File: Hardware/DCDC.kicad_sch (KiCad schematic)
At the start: 51 parts, among them Q1 100V 50A, Q2 100V 50A, Q3 100V 50A, Q4 100V 50A, U2 BQ25758A

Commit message: final tweaks before routing traces
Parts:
- C14: value 1u 25V -> 4u7u 25V
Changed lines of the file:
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@@
 	)
 	(junction
-		(at 110.49 107.95)
+		(at 109.22 107.95)
 		(diameter 0)
 		(color 0 0 0 0)
@@
 	(wire
 		(pts
-			(xy 53.34 107.95) (xy 110.49 107.95)
+			(xy 53.34 107.95) (xy 109.22 107.95)
 		)
 		(stroke
@@
 	(wire
 		(pts
-			(xy 110.49 106.68) (xy 110.49 107.95)
+			(xy 109.22 106.68) (xy 109.22 107.95)
 		)
 		(stroke
@@
 	(wire
 		(pts
-			(xy 110.49 107.95) (xy 110.49 109.22)
+			(xy 109.22 107.95) (xy 109.22 109.22)
 		)
 		(stroke
@@
 	(wire
 		(pts
+			(xy 109.22 109.22) (xy 110.49 109.22)
+		)
+		(stroke
+			(width 0)
+			(type default)
+		)
+	)
+	(wire
+		(pts
 			(xy 95.25 27.94) (xy 95.25 29.21)
 		)
@@
 	(wire
 		(pts
+			(xy 109.22 106.68) (xy 110.49 106.68)
+		)
+		(stroke
+			(width 0)
+			(type default)
+		)
+	)
+	(wire
+		(pts
 			(xy 153.67 76.2) (xy 163.83 76.2)
 		)
@@
 	(label "HIDRV1"
 		(at 125.73 91.44 90)
-		(fields_autoplaced yes)
 		(effects
 			(font
@@
 	(label "LODRV2"
 		(at 153.67 91.44 90)
-		(fields_autoplaced yes)
 		(effects
 			(font
@@
 	(label "ACP"
 		(at 105.41 101.6 0)
-		(fields_autoplaced yes)
 		(effects
 			(font
@@
 	(label "VSYS"
 		(at 125.73 29.21 0)
-		(fields_autoplaced yes)
 		(effects
 			(font
@@
 	(label "IIN"
 		(at 179.07 124.46 0)
-		(fields_autoplaced yes)
 		(effects
 			(font
@@
 	(label "SW1"
 		(at 130.81 91.44 90)
-		(fields_autoplaced yes)
 		(effects
 			(font
@@
 	(label "POUT"
 		(at 156.21 29.21 0)
-		(fields_autoplaced yes)
 		(effects
 			(font
@@
 	(label "MODE"
 		(at 179.07 129.54 0)
-		(fields_autoplaced yes)
 		(effects
 			(font
@@
 	(label "HIDRV2"
 		(at 161.29 91.44 90)
-		(fields_autoplaced yes)
 		(effects
 			(font
@@
 	(label "SW2"
 		(at 156.21 91.44 90)
-		(fields_autoplaced yes)
 		(effects
 			(font
@@
 	(label "SRP"
 		(at 179.07 99.06 0)
-		(fields_autoplaced yes)
 		(effects
 			(font
@@
 	(label "ACN"
 		(at 105.41 99.06 0)
-		(fields_autoplaced yes)
 		(effects
 			(font
@@
 	(label "BTST1"
 		(at 128.27 91.44 90)
-		(fields_autoplaced yes)
 		(effects
 			(font
@@
 	(label "LODRV1"
 		(at 133.35 91.44 90)
-		(fields_autoplaced yes)
 		(effects
 			(font
@@
 	(label "IOUT"
 		(at 179.07 127 0)
-		(fields_autoplaced yes)
 		(effects
 			(font
@@
 	(label "BTST2"
 		(at 158.75 91.44 90)
-		(fields_autoplaced yes)
 		(effects
 			(font
@@
 	(label "SRN"
 		(at 179.07 101.6 0)
-		(fields_autoplaced yes)
 		(effects
 			(font
@@
 		(shape input)
 		(at 107.95 137.16 180)
-		(fields_autoplaced yes)
 		(effects
 			(font
@@
 		(shape input)
 		(at 107.95 144.78 180)
-		(fields_autoplaced yes)
 		(effects
 			(font
@@
 		(shape input)
 		(at 257.81 27.94 90)
-		(fields_autoplaced yes)
 		(effects
 			(font
@@
 		(shape input)
 		(at 107.95 139.7 180)
-		(fields_autoplaced yes)
 		(effects
 			(font
@@
 		(shape input)
 		(at 38.1 27.94 90)
-		(fields_autoplaced yes)
 		(effects
 			(font
@@
 		(shape input)
 		(at 187.96 133.35 270)
-		(fields_autoplaced yes)
 		(effects
 			(font
@@
 		(shape input)
 		(at 107.95 142.24 180)
-		(fields_autoplaced yes)
 		(effects
 			(font
@@
 			)
 		)
-		(property "Value" "1u 25V"
+		(property "Value" "4u7u 25V"
 			(at 88.646 127.254 90)
 			(effects
@@
 				)
 				(justify left)
+				(hide yes)
 			)
 		)

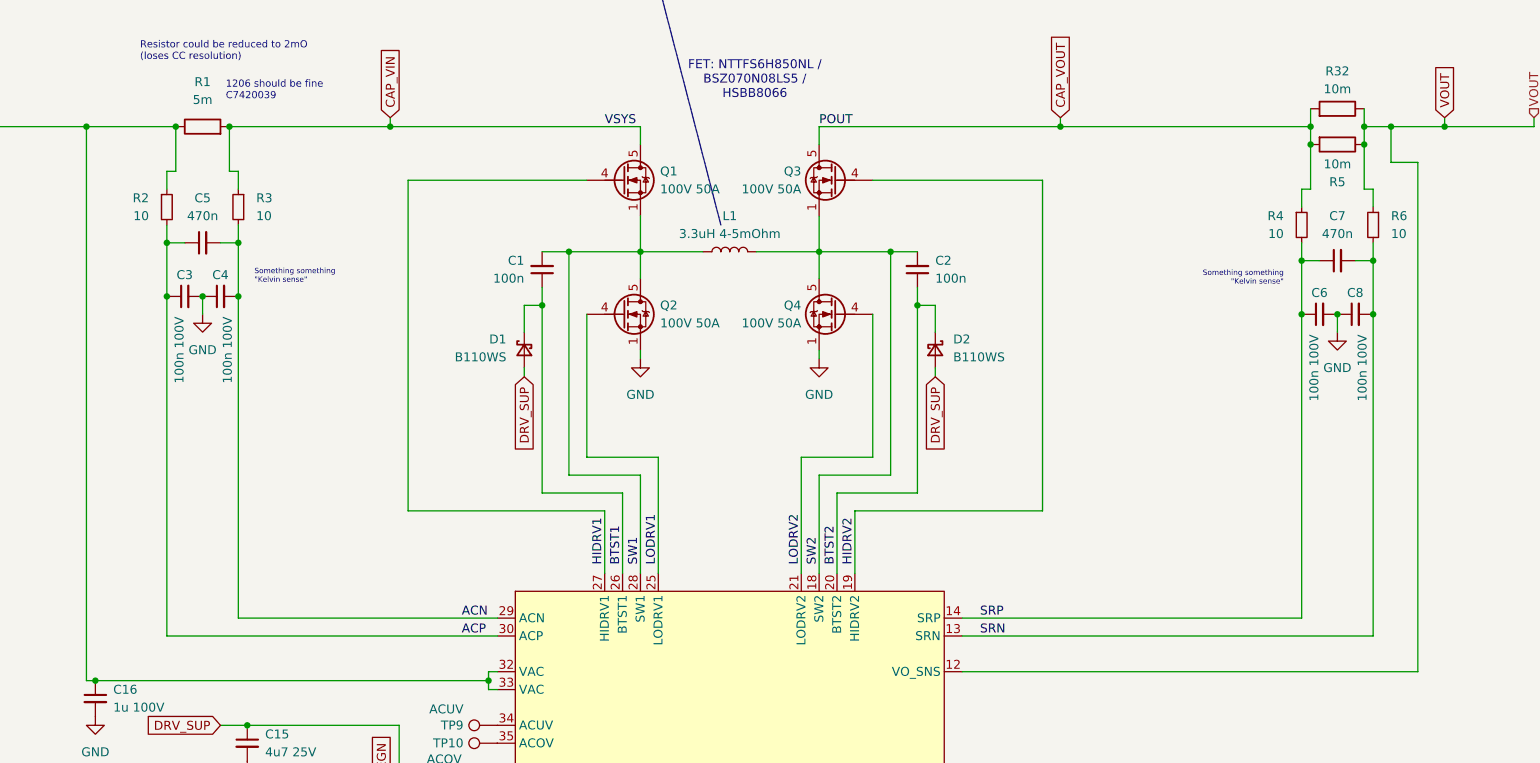
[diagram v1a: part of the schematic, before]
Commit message: main power layout almost done
UI board and details still left to do
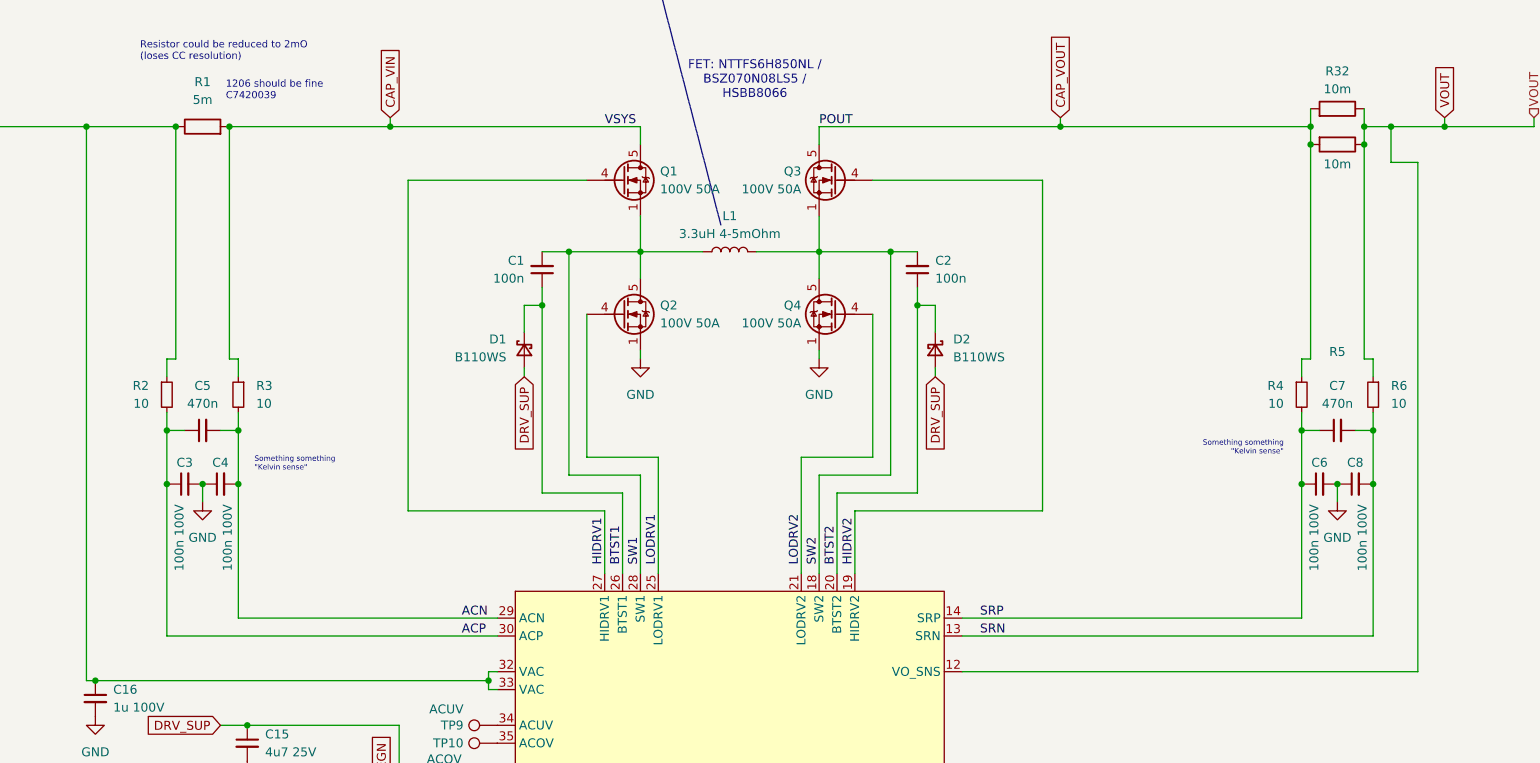
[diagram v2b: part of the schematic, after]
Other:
- moved on the sheet: C3, C4, C5, C6, C7, C8, R2, R3, R4, R6

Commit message: oops, all vias
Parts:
- TP10, TP13, TP9: now not fitted
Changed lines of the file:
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@@
 		(exclude_from_sim no)
 		(in_bom yes)
-		(on_board yes)
-		(dnp no)
+		(on_board no)
+		(dnp yes)
 		(property "Reference" "TP10"
 			(at 105.664 116.84 90)
@@
 		(exclude_from_sim no)
 		(in_bom yes)
-		(on_board yes)
-		(dnp no)
+		(on_board no)
+		(dnp yes)
 		(property "Reference" "TP13"
 			(at 185.42 136.906 90)
@@
 		(exclude_from_sim no)
 		(in_bom yes)
-		(on_board yes)
-		(dnp no)
+		(on_board no)
+		(dnp yes)
 		(property "Reference" "TP9"
 			(at 105.664 114.3 90)

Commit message: design silkscreen markings + some polish
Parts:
- removed R32: 10m, Resistor_SMD:R_1206_3216Metric, symbol Device:R
- C14: value 4u7u 25V -> 4u7 25V
- C16: footprint Capacitor_SMD:C_0402_1005Metric -> Capacitor_SMD:C_0603_1608Metric
- R5: value 10m -> 5m; footprint Resistor_SMD:R_1206_3216Metric -> Resistor_SMD:R_1020_2550Metric_Pad1.33x5.20mm_HandSolder; LCSC Part C7467248 -> C843878
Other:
- note added: "Can also place 2x 1206 10mOhm (slightly decreased accuracy)"
- moved on the sheet: R5
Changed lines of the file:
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@@
 	)
 	(junction
-		(at 226.06 31.75)
-		(diameter 0)
-		(color 0 0 0 0)
-	)
-	(junction
 		(at 44.45 179.07)
 		(diameter 0)
@@
 	)
 	(junction
-		(at 233.68 31.75)
-		(diameter 0)
-		(color 0 0 0 0)
-	)
-	(junction
 		(at 68.58 179.07)
 		(diameter 0)
@@
 	(wire
 		(pts
-			(xy 226.06 29.21) (xy 226.06 31.75)
+			(xy 226.06 29.21) (xy 226.06 62.23)
 		)
 		(stroke
@@
 	(wire
 		(pts
-			(xy 233.68 26.67) (xy 233.68 29.21)
-		)
-		(stroke
-			(width 0)
-			(type default)
-		)
-	)
-	(wire
-		(pts
 			(xy 232.41 72.39) (xy 234.95 72.39)
 		)
@@
 	(wire
 		(pts
-			(xy 226.06 31.75) (xy 226.06 62.23)
-		)
-		(stroke
-			(width 0)
-			(type default)
-		)
-	)
-	(wire
-		(pts
 			(xy 172.72 58.42) (xy 172.72 54.61)
 		)
@@
 	(wire
 		(pts
-			(xy 226.06 26.67) (xy 226.06 29.21)
-		)
-		(stroke
-			(width 0)
-			(type default)
-		)
-	)
-	(wire
-		(pts
 			(xy 234.95 80.01) (xy 234.95 101.6)
 		)
@@
 	(wire
 		(pts
-			(xy 233.68 29.21) (xy 233.68 31.75)
-		)
-		(stroke
-			(width 0)
-			(type default)
-		)
-	)
-	(wire
-		(pts
 			(xy 270.51 129.54) (xy 271.78 129.54)
 		)
@@
 	(wire
 		(pts
-			(xy 233.68 31.75) (xy 233.68 62.23)
+			(xy 233.68 29.21) (xy 233.68 62.23)
 		)
 		(stroke
@@
 		)
 	)
+	(text "Can also place \n2x 1206 10mOhm\n(slightly decreased accuracy)"
+		(exclude_from_sim no)
+		(at 227.076 24.13 0)
+		(effects
+			(font
+				(size 1.016 1.016)
+			)
+			(justify right)
+		)
+	)
 	(text "Something something\n\"Kelvin sense\""
 		(exclude_from_sim no)
@@
 			)
 		)
-		(property "Value" "4u7u 25V"
+		(property "Value" "4u7 25V"
 			(at 88.646 127.254 90)
 			(effects
@@
 	)
 	(symbol
-		(lib_id "Device:R")
-		(at 229.87 26.67 270)
-		(mirror x)
-		(unit 1)
-		(exclude_from_sim no)
-		(in_bom yes)
-		(on_board yes)
-		(dnp no)
-		(property "Reference" "R32"
-			(at 229.87 21.336 90)
-			(effects
-				(font
-					(size 1.27 1.27)
-				)
-			)
-		)
-		(property "Value" "10m"
-			(at 229.87 23.876 90)
-			(effects
-				(font
-					(size 1.27 1.27)
-				)
-			)
-		)
-		(property "Footprint" "Resistor_SMD:R_1206_3216Metric"
-			(at 229.87 28.448 90)
-			(effects
-				(font
-					(size 1.27 1.27)
-				)
-				(hide yes)
-			)
-		)
-		(property "Datasheet" "~"
-			(at 229.87 26.67 0)
-			(effects
-				(font
-					(size 1.27 1.27)
-				)
-				(hide yes)
-			)
-		)
-		(property "Description" "Resistor"
-			(at 229.87 26.67 0)
-			(effects
-				(font
-					(size 1.27 1.27)
-				)
-				(hide yes)
-			)
-		)
-		(property "LCSC" ""
-			(at 229.87 26.67 0)
-			(effects
-				(font
-					(size 1.27 1.27)
-				)
-				(hide yes)
-			)
-		)
-		(property "LCSC Part" " C7467248"
-			(at 229.87 26.67 0)
-			(effects
-				(font
-					(size 1.27 1.27)
-				)
-				(hide yes)
-			)
-		)
-		(pin "2"
-		)
-		(pin "1"
-		)
-		(instances
-			(project "USB-C PSU"
-				(path "/2795a064-4b14-4857-8c9a-fd2d32a5a222/d10f97af-4f61-4e9c-946c-7124bbc9e0fd"
-					(reference "R32")
-					(unit 1)
-				)
-			)
-		)
-	)
-	(symbol
 		(lib_id "Device:D_Schottky_Small")
 		(at 114.3 60.96 90)
@@
 			)
 		)
-		(property "Footprint" "Capacitor_SMD:C_0402_1005Metric"
+		(property "Footprint" "Capacitor_SMD:C_0603_1608Metric"
 			(at 53.34 110.49 0)
 			(effects
@@
 	(symbol
 		(lib_id "Device:R")
-		(at 229.87 31.75 270)
+		(at 229.87 29.21 270)
 		(unit 1)
 		(exclude_from_sim no)
@@
 		(dnp no)
 		(property "Reference" "R5"
-			(at 229.87 61.214 90)
+			(at 229.87 24.13 90)
 			(effects
 				(font
@@
 			)
 		)
-		(property "Value" "10m"
-			(at 229.87 34.544 90)
+		(property "Value" "5m"
+			(at 229.87 26.67 90)
 			(effects
 				(font
@@
 			)
 		)
-		(property "Footprint" "Resistor_SMD:R_1206_3216Metric"
-			(at 229.87 29.972 90)
+		(property "Footprint" "Resistor_SMD:R_1020_2550Metric_Pad1.33x5.20mm_HandSolder"
+			(at 229.87 27.432 90)
 			(effects
 				(font
@@
 		)
 		(property "Datasheet" "~"
-			(at 229.87 31.75 0)
+			(at 229.87 29.21 0)
 			(effects
 				(font
@@
 		)
 		(property "Description" "Resistor"
-			(at 229.87 31.75 0)
+			(at 229.87 29.21 0)
 			(effects
 				(font
@@
 		)
 		(property "LCSC" ""
-			(at 229.87 31.75 0)
+			(at 229.87 29.21 0)
 			(effects
 				(font
@@
 			)
 		)
-		(property "LCSC Part" " C7467248"
-			(at 229.87 31.75 0)
+		(property "LCSC Part" "C843878"
+			(at 229.87 29.21 0)
 			(effects
 				(font
